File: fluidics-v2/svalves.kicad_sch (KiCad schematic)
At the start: 9 parts, among them IC2 ADUM1250WSRZ-RL7, U6 LTC4311CSC6-TRPBF

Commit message: V3: strip to minimal fluidics config, add 6th selector valve, fix lib paths
Reduce the V2 fluidics controller to a minimal build and extend the
selector-valve bank:

- Remove disc-pump driver (U1, M1); keep the syringe pump only
- Remove the solenoid-valve subsystem (MCZ33996 IC1 + D5-D20 + R6-R21
  + connector J5) -- 16 solenoids -> 0
- Remove all SPI pressure sensors (IC3-IC6 and their passives) -- 4 -> 0
- Reduce I2C flow sensors 4 -> 3 (drop connector J17)
- Add a 6th IDEX selector-valve channel (connectors J24/J25) on the
  shared isolated-I2C + 24V bus
- Remove the Wenzel-lab pressure-controller daughter board interface
  (J6, J7/ICSP, J8, JP3)
- Remove the manual-control block (switches S1-S4, push-button SW1,
  potentiometer VR1, TCA9539 U7, pull-ups, jumpers)
- Remove the 24V->12V converter (U5 + indicator D1/R2 + power-good R52);
  no remaining 12V load after the above

Net component count: 177 -> 86 footprints. DRC: 0 unconnected.

Tooling/portability fixes:
- Rewrite fp-lib-table and sym-lib-table: replace the original author's
  hardcoded absolute paths (/home/octopi-codex/...) with ${KIPRJMOD}-
  relative URIs so the libraries resolve on any machine
- Migrate the project to KiCad 10 format
- Add .gitignore for KiCad lock/autosave/cache and editor history files
- Add fluidics-v3-schematic.pdf (rendered schematic for review)

Co-Authored-By: Claude Opus 4.8 (1M context) <noreply@anthropic.com>
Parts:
- gave numbers to parts that had none: 7

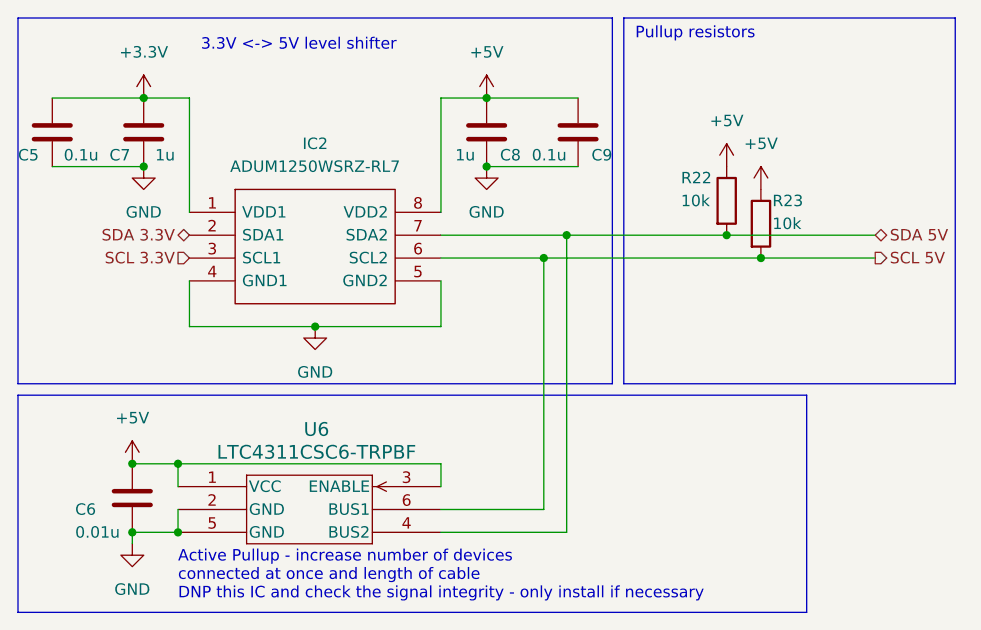
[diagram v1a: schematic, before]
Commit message: PCB fix: add R1 (svalves), clear dangling track; refresh schematic PDF
- Add resistor R1 on svalves sheet, placed on board; footprints 76 -> 77.
- Prior dangling J6 track resolved (DRC track_dangling now 0).
- DRC: schematic_parity 0, 5 intentional no-connects, rest cosmetic
  (silk/courtyard/padstack inherited from upstream).
- Regenerate fluidics-v3-schematic.pdf from current schematic.

Co-Authored-By: Claude Opus 4.8 (1M context) <noreply@anthropic.com>
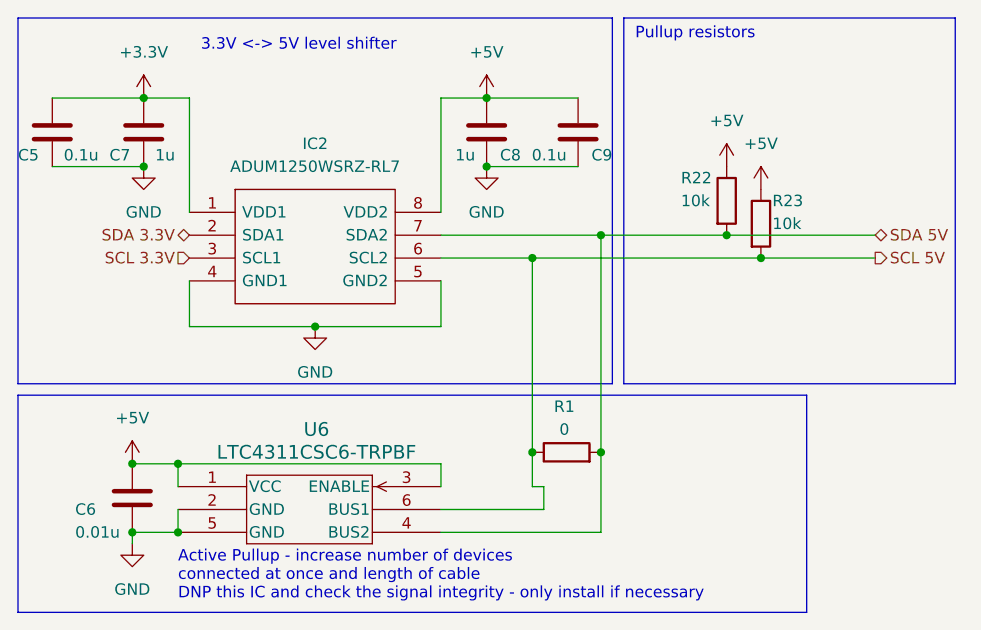
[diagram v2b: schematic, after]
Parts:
- added R1: 0, Resistor_SMD:R_0402_1005Metric, symbol Device:R
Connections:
- net SCL 5V: now also R1.1
- net SDA 5V: now also R1.2
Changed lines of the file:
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@@
-	)
-	(junction
-		(at 106.68 54.61)
-		(diameter 0)
-		(color 0 0 0 0)
 	)
 	(junction
@@
 	)
 	(junction
+		(at 110.49 78.74)
+		(diameter 0)
+		(color 0 0 0 0)
+	)
+	(junction
 		(at 63.5 87.63)
 		(diameter 0)
@@
 	)
 	(junction
-		(at 104.14 57.15)
-		(diameter 0)
-		(color 0 0 0 0)
-	)
-	(junction
 		(at 58.42 87.63)
 		(diameter 0)
@@
 	)
 	(junction
+		(at 102.87 57.15)
+		(diameter 0)
+		(color 0 0 0 0)
+	)
+	(junction
+		(at 110.49 54.61)
+		(diameter 0)
+		(color 0 0 0 0)
+	)
+	(junction
 		(at 128.27 57.15)
 		(diameter 0)
@@
 	)
 	(junction
+		(at 102.87 78.74)
+		(diameter 0)
+		(color 0 0 0 0)
+	)
+	(junction
 		(at 124.46 54.61)
 		(diameter 0)
@@
 	(wire
 		(pts
+			(xy 102.87 78.74) (xy 102.87 57.15)
+		)
+		(stroke
+			(width 0)
+			(type default)
+		)
+	)
+	(wire
+		(pts
 			(xy 49.53 39.37) (xy 59.69 39.37)
 		)
@@
 	(wire
 		(pts
+			(xy 110.49 54.61) (xy 110.49 78.74)
+		)
+		(stroke
+			(width 0)
+			(type default)
+		)
+	)
+	(wire
+		(pts
 			(xy 107.95 46.99) (xy 97.79 46.99)
 		)
@@
 	(wire
 		(pts
+			(xy 102.87 82.55) (xy 102.87 78.74)
+		)
+		(stroke
+			(width 0)
+			(type default)
+		)
+	)
+	(wire
+		(pts
 			(xy 64.77 59.69) (xy 64.77 64.77)
 		)
@@
 	(wire
 		(pts
-			(xy 104.14 57.15) (xy 128.27 57.15)
-		)
-		(stroke
-			(width 0)
-			(type default)
-		)
-	)
-	(wire
-		(pts
-			(xy 106.68 87.63) (xy 92.71 87.63)
-		)
-		(stroke
-			(width 0)
-			(type default)
-		)
-	)
-	(wire
-		(pts
-			(xy 106.68 54.61) (xy 106.68 87.63)
-		)
-		(stroke
-			(width 0)
-			(type default)
-		)
-	)
-	(wire
-		(pts
-			(xy 104.14 85.09) (xy 104.14 57.15)
+			(xy 92.71 87.63) (xy 110.49 87.63)
+		)
+		(stroke
+			(width 0)
+			(type default)
+		)
+	)
+	(wire
+		(pts
+			(xy 104.14 82.55) (xy 102.87 82.55)
 		)
 		(stroke
@@
 	(wire
 		(pts
-			(xy 106.68 54.61) (xy 124.46 54.61)
-		)
-		(stroke
-			(width 0)
-			(type default)
-		)
-	)
-	(wire
-		(pts
 			(xy 92.71 85.09) (xy 104.14 85.09)
 		)
@@
 	(wire
 		(pts
+			(xy 104.14 85.09) (xy 104.14 82.55)
+		)
+		(stroke
+			(width 0)
+			(type default)
+		)
+	)
+	(wire
+		(pts
 			(xy 124.46 54.61) (xy 140.97 54.61)
 		)
@@
 	(wire
 		(pts
-			(xy 92.71 54.61) (xy 106.68 54.61)
+			(xy 102.87 57.15) (xy 128.27 57.15)
+		)
+		(stroke
+			(width 0)
+			(type default)
+		)
+	)
+	(wire
+		(pts
+			(xy 92.71 54.61) (xy 110.49 54.61)
 		)
 		(stroke
@@
 	(wire
 		(pts
-			(xy 104.14 57.15) (xy 92.71 57.15)
+			(xy 92.71 57.15) (xy 102.87 57.15)
 		)
 		(stroke
@@
 		(pts
 			(xy 63.5 80.01) (xy 63.5 82.55)
+		)
+		(stroke
+			(width 0)
+			(type default)
+		)
+	)
+	(wire
+		(pts
+			(xy 110.49 54.61) (xy 124.46 54.61)
+		)
+		(stroke
+			(width 0)
+			(type default)
+		)
+	)
+	(wire
+		(pts
+			(xy 110.49 78.74) (xy 110.49 87.63)
 		)
 		(stroke
@@
 					(unit 1)
 				)
+			)
+		)
+	)
+	(symbol
+		(lib_id "Device:R")
+		(at 106.68 78.74 90)
+		(unit 1)
+		(body_style 1)
+		(exclude_from_sim no)
+		(in_bom yes)
+		(on_board yes)
+		(in_pos_files yes)
+		(dnp no)
+		(property "Reference" "R1"
+			(at 106.426 73.66 90)
+			(show_name no)
+			(do_not_autoplace no)
+			(effects
+				(font
+					(size 1.27 1.27)
+				)
+			)
+		)
+		(property "Value" "0"
+			(at 106.426 76.2 90)
+			(show_name no)
+			(do_not_autoplace no)
+			(effects
+				(font
+					(size 1.27 1.27)
+				)
+			)
+		)
+		(property "Footprint" "Resistor_SMD:R_0402_1005Metric"
+			(at 106.68 80.518 90)
+			(hide yes)
+			(show_name no)
+			(do_not_autoplace no)
+			(effects
+				(font
+					(size 1.27 1.27)
+				)
+			)
+		)
+		(property "Datasheet" ""
+			(at 106.68 78.74 0)
+			(hide yes)
+			(show_name no)
+			(do_not_autoplace no)
+			(effects
+				(font
+					(size 1.27 1.27)
+				)
+			)
+		)
+		(property "Description" "Resistor"
+			(at 106.68 78.74 0)
+			(hide yes)
+			(show_name no)
+			(do_not_autoplace no)
+			(effects
+				(font
+					(size 1.27 1.27)
+				)
+			)
+		)
+		(pin "2"
+		)
+		(pin "1"
+		)
+		(instances
+			(project "fluidics-v2"
+				(path "/0ec91c42-8aad-437d-8c85-5e10f0e51fe0/7edd626f-fd99-40ee-aab3-2aaadfd0b2bc"
+					(reference "R1")
+					(unit 1)
+				)
